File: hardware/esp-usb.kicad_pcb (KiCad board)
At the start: 2 copper layers, 30 x 18 mm, 29 parts, among them J1 USB_A, J2 Conn_01x05, J3 Conn_01x05, J4 USB_A, SW1 SW_Push, U1 ESP32-C3, U2 SPX3819M5-L-3-3, U7 TPD2EUSB30A, Y1 Crystal_GND23

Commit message: Use IRL pic
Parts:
- turned D1 to 180 degrees
- turned D2 to 180 degrees
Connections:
- D1 pad 1: /GPIO3 -> Net-(D1-K)
- D1 pad 2: Net-(D1-A) -> /GPIO3
- D2 pad 1: /GPIO4 -> Net-(D2-K)
- D2 pad 2: Net-(D2-A) -> /GPIO4
- R2 pad 1: Net-(D2-A) -> Net-(D2-K)
- R3 pad 1: Net-(D1-A) -> Net-(D1-K)
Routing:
- net GND: track 0.36 -> 4.95 mm
- net Net-(D1-K): track 0.00 -> 3.33 mm, vias 0 -> 2
- net Net-(D1-A): track 3.33 -> 0.00 mm, vias 2 -> 0
- net Net-(D2-K): track 0.00 -> 3.21 mm
- net Net-(D2-A): track 3.21 -> 0.00 mm
- net /D-: track 23.9 -> 23.1 mm
- net /D+: track 25.6 -> 24.9 mm

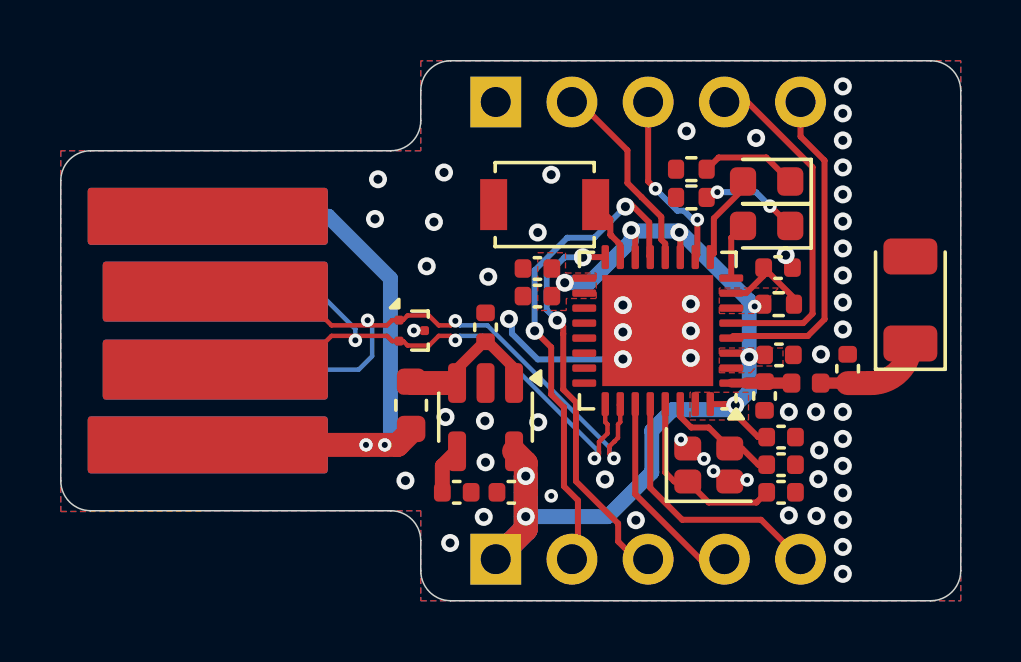
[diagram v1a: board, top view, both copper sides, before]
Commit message: Remove back fill
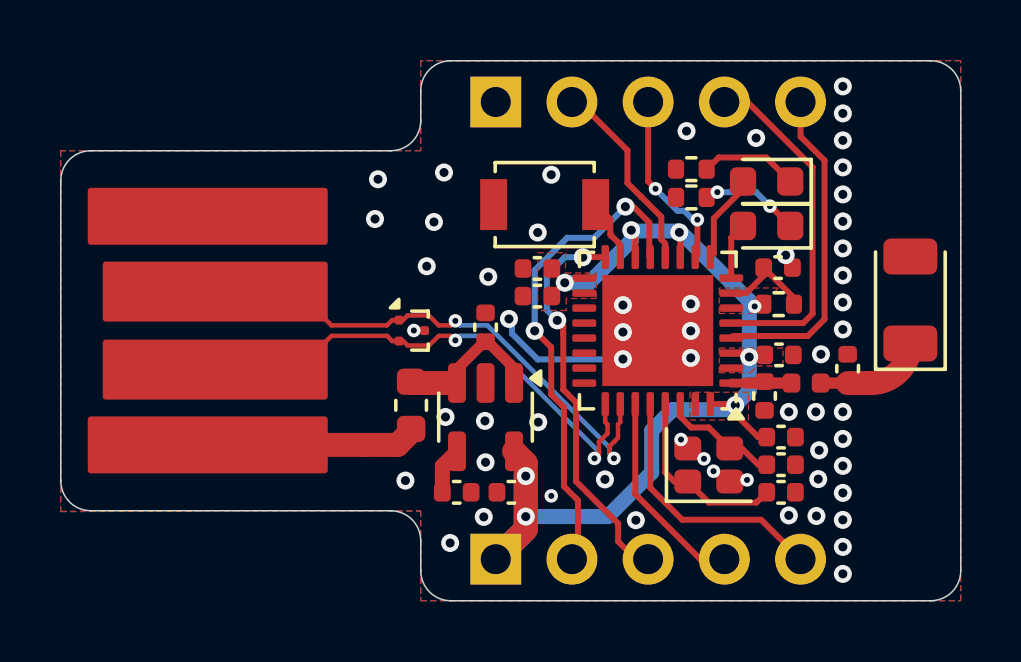
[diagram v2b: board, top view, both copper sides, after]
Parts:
- removed J4: USB_A, esp-usb-lib:USBPCB
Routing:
- net Net-(J1-VBUS): track 20.2 -> 7.02 mm, vias 2 -> 0
- net /D+: track 24.9 -> 18.2 mm, vias 3 -> 2
- net /D-: track 23.1 -> 17.5 mm, vias 3 -> 2
